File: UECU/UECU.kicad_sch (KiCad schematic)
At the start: 43 parts, among them J1 Conn_display, J1 Conn_pwr, J3 Conn_SENSORS, P1 LM2596_buck, T1 LoRa-SX1276, U1 4N25, U2 4N25, U3 4N25

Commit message: add front layer
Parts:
- removed H5, H6: 3.7, MountingHole:MountingHole_3.7mm, symbol Mechanical:MountingHole
- R1, R2, R3, R5, R6, R8, R9: footprint Resistor_THT:R_Axial_DIN0204_L3.6mm_D1.6mm_P5.08mm_Horizontal -> Resistor_THT:R_Axial_DIN0207_L6.3mm_D2.5mm_P7.62mm_Horizontal
- R7: value 2K -> 2k; footprint Resistor_THT:R_Axial_DIN0204_L3.6mm_D1.6mm_P5.08mm_Horizontal -> Resistor_THT:R_Axial_DIN0207_L6.3mm_D2.5mm_P7.62mm_Horizontal
- S1: footprint Connector_PinHeader_2.54mm:PinHeader_1x08_P2.54mm_Horizontal -> Connector_PinHeader_2.54mm:PinHeader_1x08_P2.54mm_Vertical
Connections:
- net +12V: now also C3.1, C4.1
- net +5V: no longer C3.1, C4.1
- net GND: now also D1.1 (K); no longer R3.2
- net LED_ALIVE: now also R3.1; no longer D1.2 (A)
- net RXD2: now also J1.2 (Pin_2); no longer J1.3 (Pin_3)
- net TXD2: now also J1.3 (Pin_3); no longer J1.2 (Pin_2)
- new net: D1.2 (A), R3.2
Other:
- note removed: "(Front)"
- note removed: "(Rear)"
- moved on the sheet: C3, C4, C5, C6, D1, H1, H2, H3, H4, R3

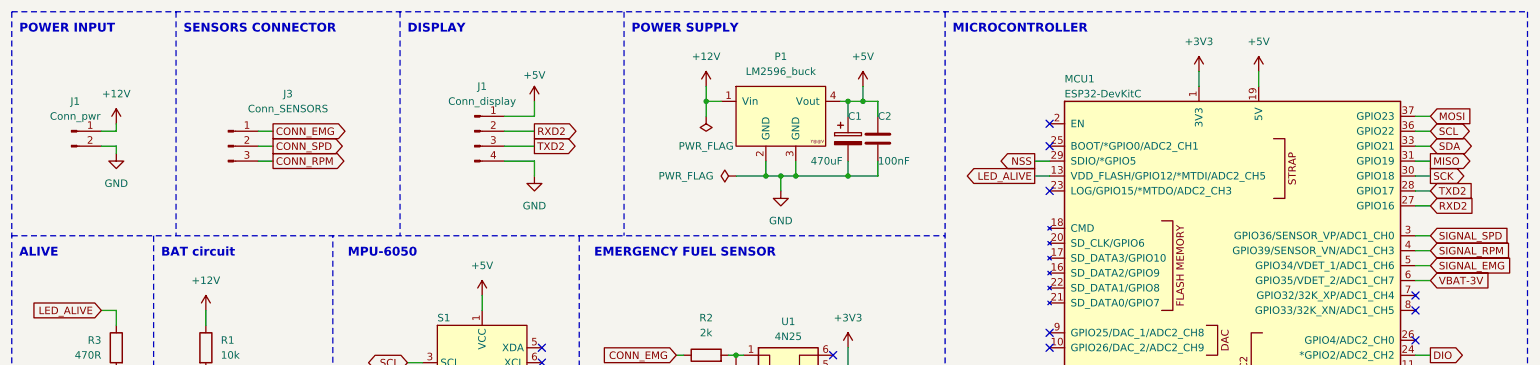
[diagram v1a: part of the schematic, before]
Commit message: finish bottom layer
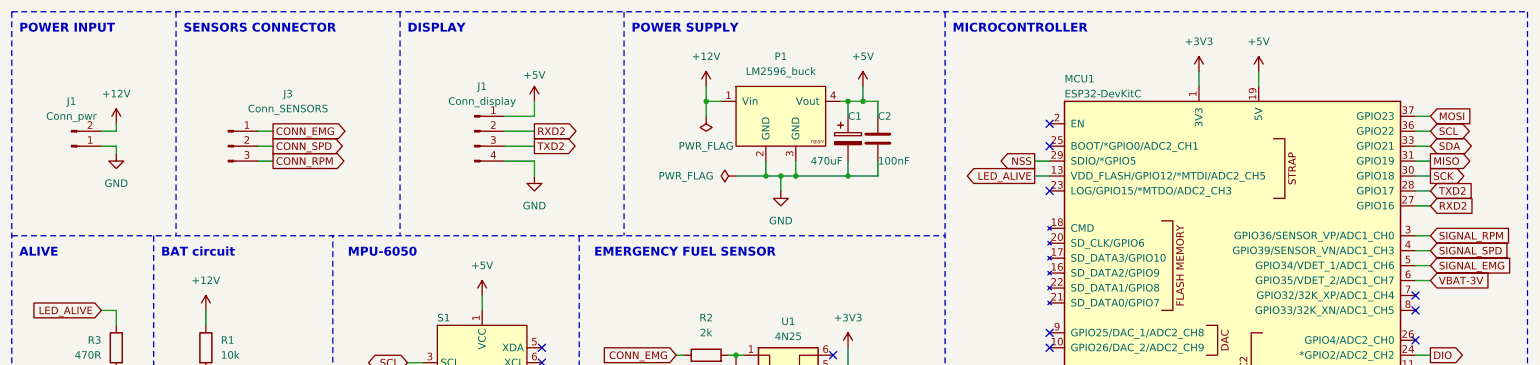
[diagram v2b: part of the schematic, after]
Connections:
- net +12V: now also J1.2 (Pin_2); no longer J1.1 (Pin_1)
- net GND: now also J1.1 (Pin_1); no longer J1.2 (Pin_2)
- net SIGNAL_RPM: now also MCU1.3 (GPIO36/SENSOR_VP/ADC1_CH0); no longer MCU1.4 (GPIO39/SENSOR_VN/ADC1_CH3)
- net SIGNAL_SPD: now also MCU1.4 (GPIO39/SENSOR_VN/ADC1_CH3); no longer MCU1.3 (GPIO36/SENSOR_VP/ADC1_CH0)
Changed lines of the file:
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@@
     )
   )
-  (global_label "SIGNAL_RPM" (shape input) (at 257.81 74.93 0) (fields_autoplaced)
-    (effects (font (size 1.27 1.27)) (justify left))
-    (property "Intersheetrefs" "${INTERSHEET_REFS}" (at 272.2857 74.93 0)
+  (global_label "SIGNAL_RPM" (shape input) (at 257.81 72.39 0) (fields_autoplaced)
+    (effects (font (size 1.27 1.27)) (justify left))
+    (property "Intersheetrefs" "${INTERSHEET_REFS}" (at 272.2857 72.39 0)
       (effects (font (size 1.27 1.27)) (justify left) hide)
     )
@@
     )
   )
-  (global_label "SIGNAL_SPD" (shape input) (at 257.81 72.39 0) (fields_autoplaced)
-    (effects (font (size 1.27 1.27)) (justify left))
-    (property "Intersheetrefs" "${INTERSHEET_REFS}" (at 272.0438 72.39 0)
+  (global_label "SIGNAL_SPD" (shape input) (at 257.81 74.93 0) (fields_autoplaced)
+    (effects (font (size 1.27 1.27)) (justify left))
+    (property "Intersheetrefs" "${INTERSHEET_REFS}" (at 272.0438 74.93 0)
       (effects (font (size 1.27 1.27)) (justify left) hide)
     )
@@
     )
   )
-  (symbol (lib_id "Connector:Conn_01x02_Pin") (at 26.67 54.61 0) (unit 1)
-    (in_bom yes) (on_board yes) (dnp no) (fields_autoplaced)
-    (property "Reference" "J1" (at 27.305 49.53 0)
-      (effects (font (size 1.27 1.27)))
-    )
-    (property "Value" "Conn_pwr" (at 27.305 52.07 0)
-      (effects (font (size 1.27 1.27)))
-    )
-    (property "Footprint" "Connector_JST:JST_XH_B2B-XH-A_1x02_P2.50mm_Vertical" (at 26.67 54.61 0)
-      (effects (font (size 1.27 1.27)) hide)
-    )
-    (property "Datasheet" "~" (at 26.67 54.61 0)
-      (effects (font (size 1.27 1.27)) hide)
-    )
+  (symbol (lib_id "Connector:Conn_01x02_Pin") (at 26.67 57.15 0) (mirror x) (unit 1)
+    (in_bom yes) (on_board yes) (dnp no)
+    (property "Reference" "J1" (at 26.67 49.53 0)
+      (effects (font (size 1.27 1.27)))
+    )
+    (property "Value" "Conn_pwr" (at 26.67 52.07 0)
+      (effects (font (size 1.27 1.27)))
+    )
+    (property "Footprint" "Connector_JST:JST_XH_B2B-XH-A_1x02_P2.50mm_Vertical" (at 26.67 57.15 0)
+      (effects (font (size 1.27 1.27)) hide)
+    )
+    (property "Datasheet" "~" (at 26.67 57.15 0)
+      (effects (font (size 1.27 1.27)) hide)
+    )

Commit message: create new module
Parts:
- added L1: ~, Logos:parahybaja, symbol Logos:parahybaja
- added L2: ~, Logos:open_hardware, symbol Logos:open-hardware
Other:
- moved on the sheet: H1, H2, H3, H4
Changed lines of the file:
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@@
   (title_block
     (title "UECU")
-    (date "2023-12-28")
-    (rev "v2.2")
+    (date "2023-12-29")
+    (rev "v2.4")
     (company "Parahybaja")
     (comment 1 "by Jefferson Lopes")
@@
     )
   )
+  (symbol (lib_id "Logos:parahybaja") (at 35.56 173.99 0) (unit 1)
+    (in_bom yes) (on_board yes) (dnp no) (fields_autoplaced)
+    (property "Reference" "L1" (at 40.64 172.72 0)
+      (effects (font (size 1.27 1.27)))
+    )
+    (property "Value" "~" (at 35.56 173.99 0)
+      (effects (font (size 1.27 1.27)))
+    )
+    (property "Footprint" "Logos:parahybaja" (at 40.64 179.07 0)
+      (effects (font (size 1.27 1.27)) hide)
+    )
+    (property "Datasheet" "" (at 35.56 173.99 0)
+      (effects (font (size 1.27 1.27)) hide)
+    )
+    (instances
+      (project "UECU"
+        (path "/78df87d8-4be6-423b-b1b3-5ac2954b2e61"
+          (reference "L1") (unit 1)
+        )
+      )
+    )
+  )
   (symbol (lib_name "GND_7") (lib_id "power:GND") (at 128.27 176.53 0) (unit 1)
     (in_bom yes) (on_board yes) (dnp no) (fields_autoplaced)
@@
     )
   )
-  (symbol (lib_id "Mechanical:MountingHole") (at 41.91 168.91 0) (unit 1)
+  (symbol (lib_id "Mechanical:MountingHole") (at 41.91 165.1 0) (unit 1)
     (in_bom yes) (on_board yes) (dnp no) (fields_autoplaced)
-    (property "Reference" "H2" (at 44.45 167.64 0)
+    (property "Reference" "H2" (at 44.45 163.83 0)
       (effects (font (size 1.27 1.27)) (justify left))
     )
-    (property "Value" "3.7" (at 44.45 170.18 0)
+    (property "Value" "3.7" (at 44.45 166.37 0)
       (effects (font (size 1.27 1.27)) (justify left))
     )
-    (property "Footprint" "MountingHole:MountingHole_3.7mm" (at 41.91 168.91 0)
+    (property "Footprint" "MountingHole:MountingHole_3.7mm" (at 41.91 165.1 0)
       (effects (font (size 1.27 1.27)) hide)
     )
-    (property "Datasheet" "~" (at 41.91 168.91 0)
+    (property "Datasheet" "~" (at 41.91 165.1 0)
       (effects (font (size 1.27 1.27)) hide)
     )
@@
     )
   )
-  (symbol (lib_id "Mechanical:MountingHole") (at 27.94 168.91 0) (unit 1)
+  (symbol (lib_id "Mechanical:MountingHole") (at 27.94 165.1 0) (unit 1)
     (in_bom yes) (on_board yes) (dnp no) (fields_autoplaced)
-    (property "Reference" "H1" (at 31.115 167.64 0)
+    (property "Reference" "H1" (at 31.115 163.83 0)
       (effects (font (size 1.27 1.27)) (justify left))
     )
-    (property "Value" "3.7" (at 31.115 170.18 0)
+    (property "Value" "3.7" (at 31.115 166.37 0)
       (effects (font (size 1.27 1.27)) (justify left))
     )
-    (property "Footprint" "MountingHole:MountingHole_3.7mm" (at 27.94 168.91 0)
+    (property "Footprint" "MountingHole:MountingHole_3.7mm" (at 27.94 165.1 0)
       (effects (font (size 1.27 1.27)) hide)
     )
-    (property "Datasheet" "~" (at 27.94 168.91 0)
+    (property "Datasheet" "~" (at 27.94 165.1 0)
       (effects (font (size 1.27 1.27)) hide)
     )
@@
     )
   )
+  (symbol (lib_id "Logos:open-hardware") (at 57.15 173.99 0) (unit 1)
+    (in_bom yes) (on_board yes) (dnp no)
+    (property "Reference" "L2" (at 60.96 172.72 0)
+      (effects (font (size 1.27 1.27)) (justify left))
+    )
+    (property "Value" "~" (at 57.15 173.99 0)
+      (effects (font (size 1.27 1.27)))
+    )
+    (property "Footprint" "Logos:open_hardware" (at 62.23 180.34 0)
+      (effects (font (size 1.27 1.27)) hide)
+    )
+    (property "Datasheet" "" (at 57.15 173.99 0)
+      (effects (font (size 1.27 1.27)) hide)
+    )
+    (instances
+      (project "UECU"
+        (path "/78df87d8-4be6-423b-b1b3-5ac2954b2e61"
+          (reference "L2") (unit 1)
+        )
+      )
+    )
+  )
   (symbol (lib_id "power:+3V3") (at 160.02 163.83 0) (unit 1)
     (in_bom yes) (on_board yes) (dnp no) (fields_autoplaced)
@@
     )
   )
-  (symbol (lib_id "Mechanical:MountingHole") (at 67.31 168.91 0) (unit 1)
+  (symbol (lib_id "Mechanical:MountingHole") (at 67.31 165.1 0) (unit 1)
     (in_bom yes) (on_board yes) (dnp no) (fields_autoplaced)
-    (property "Reference" "H4" (at 70.485 167.64 0)
+    (property "Reference" "H4" (at 70.485 163.83 0)
       (effects (font (size 1.27 1.27)) (justify left))
     )
-    (property "Value" "3.7" (at 70.485 170.18 0)
+    (property "Value" "3.7" (at 70.485 166.37 0)
       (effects (font (size 1.27 1.27)) (justify left))
     )
-    (property "Footprint" "MountingHole:MountingHole_3.7mm" (at 67.31 168.91 0)
+    (property "Footprint" "MountingHole:MountingHole_3.7mm" (at 67.31 165.1 0)
       (effects (font (size 1.27 1.27)) hide)
     )
-    (property "Datasheet" "~" (at 67.31 168.91 0)
+    (property "Datasheet" "~" (at 67.31 165.1 0)
       (effects (font (size 1.27 1.27)) hide)
     )
@@
     )
   )
-  (symbol (lib_id "Mechanical:MountingHole") (at 54.61 168.91 0) (unit 1)
+  (symbol (lib_id "Mechanical:MountingHole") (at 54.61 165.1 0) (unit 1)
     (in_bom yes) (on_board yes) (dnp no) (fields_autoplaced)
-    (property "Reference" "H3" (at 57.15 167.64 0)
+    (property "Reference" "H3" (at 57.15 163.83 0)
       (effects (font (size 1.27 1.27)) (justify left))
     )
-    (property "Value" "3.7" (at 57.15 170.18 0)
+    (property "Value" "3.7" (at 57.15 166.37 0)
       (effects (font (size 1.27 1.27)) (justify left))
     )
-    (property "Footprint" "MountingHole:MountingHole_3.7mm" (at 54.61 168.91 0)
+    (property "Footprint" "MountingHole:MountingHole_3.7mm" (at 54.61 165.1 0)
       (effects (font (size 1.27 1.27)) hide)
     )
-    (property "Datasheet" "~" (at 54.61 168.91 0)
+    (property "Datasheet" "~" (at 54.61 165.1 0)
       (effects (font (size 1.27 1.27)) hide)
     )
